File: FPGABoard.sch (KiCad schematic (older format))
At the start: 0 parts

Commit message: Layout
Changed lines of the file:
@@
 LIBS:switches
 LIBS:xo-14s
+LIBS:oscillator_xo
 LIBS:FPGABoard-cache
 EELAYER 25 0
@@
 F10 "CS_Controller" O L 6350 5450 60
 F11 "CS_FPGA" I L 6350 5650 60
-F12 "Clock_In" I L 6350 4900 60
-F13 "INIT_B" I L 6350 6050 60
-F14 "DONE" O L 6350 5950 60
-F15 "PROG_B" B L 6350 5850 60
-F16 "GPIO0[1..12]" B R 8450 5350 60
-F17 "GPIO3[1..10]" B R 8450 5650 60
+F12 "INIT_B" I L 6350 6050 60
+F13 "DONE" O L 6350 5950 60
+F14 "PROG_B" B L 6350 5850 60
+F15 "GPIO0[1..12]" B R 8450 5350 60
+F16 "GPIO3[1..10]" B R 8450 5650 60
 $EndSheet
 $Sheet
@@
 F6 "GPIO2[1..12]" B L 9850 5550 60
 F7 "GPIO3[1..10]" B L 9850 5650 60
-F8 "C_IO[1..6]" B L 9850 6650 60
+F8 "C_IO[1..4]" B L 9850 6650 60
 $EndSheet
 Wire Wire Line
@@
 Wire Wire Line
 	4900 5650 6350 5650
-Wire Wire Line
-	6350 4900 4900 4900
 Wire Wire Line
 	4900 5850 6350 5850
@@
 F10 "DONE" I R 4900 5950 60
 F11 "INIT_B" I R 4900 6050 60
-F12 "Clock_Out" O R 4900 4900 60
-F13 "C_IO[1..6]" B R 4900 6550 60
+F12 "C_IO[1..4]" B R 4900 6550 60
 $EndSheet
 Wire Bus Line

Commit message: Ready for Production
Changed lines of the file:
@@
 EESchema Schematic File Version 2
+LIBS:FPGABoard-rescue
 LIBS:power
 LIBS:device
@@
 F16 "GPIO3[1..10]" B R 8450 5650 60
 $EndSheet
-$Sheet
-S 9850 4250 1850 2750
-U 5748D767
-F0 "Connections" 60
-F1 "Connections.sch" 60
-F2 "LED[1..3]" I L 9850 5150 60
-F3 "BTN[1..2]" O L 9850 5250 60
-F4 "GPIO0[1..12]" B L 9850 5350 60
-F5 "GPIO1[1..12]" B L 9850 5450 60
-F6 "GPIO2[1..12]" B L 9850 5550 60
-F7 "GPIO3[1..10]" B L 9850 5650 60
-F8 "C_IO[1..4]" B L 9850 6650 60
-$EndSheet
 Wire Wire Line
 	3100 4450 2850 4450
@@
 F10 "DONE" I R 4900 5950 60
 F11 "INIT_B" I R 4900 6050 60
-F12 "C_IO[1..4]" B R 4900 6550 60
 $EndSheet
 Wire Bus Line
@@
 F2 "V_USB" I L 3150 1900 60
 $EndSheet
-Wire Bus Line
-	4900 6550 5600 6550
-Wire Bus Line
-	5600 6550 5600 7550
-Wire Bus Line
-	5600 7550 9150 7550
-Wire Bus Line
-	9150 7550 9150 6650
-Wire Bus Line
-	9150 6650 9850 6650
+$Sheet
+S 9850 4250 1850 2750
+U 5748D767
+F0 "Connections" 60
+F1 "Connections.sch" 60
+F2 "LED[1..3]" I L 9850 5150 60
+F3 "BTN[1..2]" O L 9850 5250 60
+F4 "GPIO0[1..12]" B L 9850 5350 60
+F5 "GPIO1[1..12]" B L 9850 5450 60
+F6 "GPIO2[1..12]" B L 9850 5550 60
+F7 "GPIO3[1..10]" B L 9850 5650 60
+$EndSheet
 $EndSCHEMATC

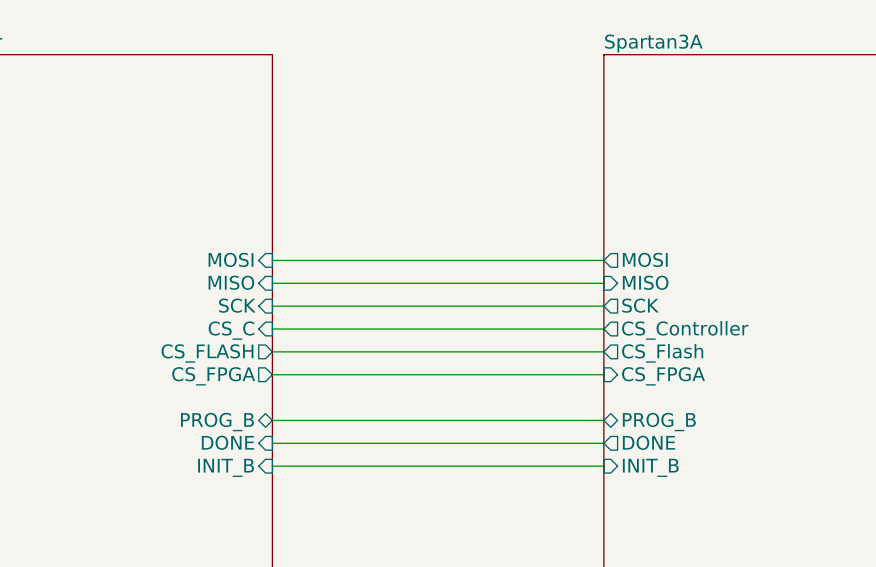
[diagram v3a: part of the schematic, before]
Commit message: Changed SPI Connection to support Multi-Master
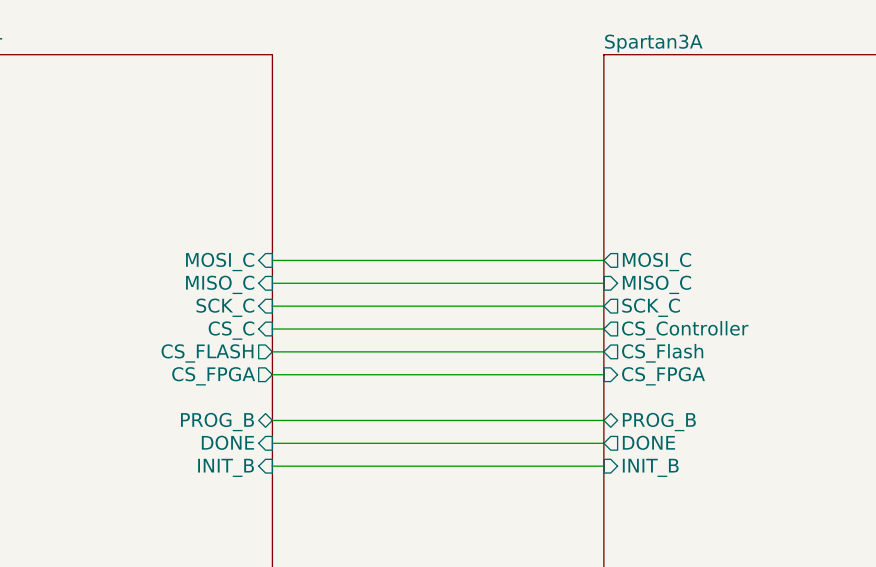
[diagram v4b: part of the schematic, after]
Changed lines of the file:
@@
 F0 "Spartan3A" 60
 F1 "Spartan3A.sch" 60
-F2 "MISO" I L 6350 5250 60
-F3 "SCK" O L 6350 5350 60
+F2 "MISO_C" I L 6350 5250 60
+F3 "SCK_C" O L 6350 5350 60
 F4 "CS_Flash" O L 6350 5550 60
-F5 "MOSI" O L 6350 5150 60
+F5 "MOSI_C" O L 6350 5150 60
 F6 "LED[1..3]" O R 8450 5150 60
 F7 "BTN[1..2]" I R 8450 5250 60
@@
 F0 "Microcontroller" 60
 F1 "Microcontroller.sch" 60
-F2 "MOSI" I R 4900 5150 60
-F3 "MISO" I R 4900 5250 60
-F4 "SCK" I R 4900 5350 60
+F2 "MOSI_C" I R 4900 5150 60
+F3 "MISO_C" I R 4900 5250 60
+F4 "SCK_C" I R 4900 5350 60
 F5 "CS_C" I R 4900 5450 60
 F6 "V_USB" O L 3100 4450 60
